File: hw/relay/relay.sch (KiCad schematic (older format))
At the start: 14 parts, among them J1 trigger input, J2 power input, J3 output terminal, K1 G5LE-1, Q1 PN2222A

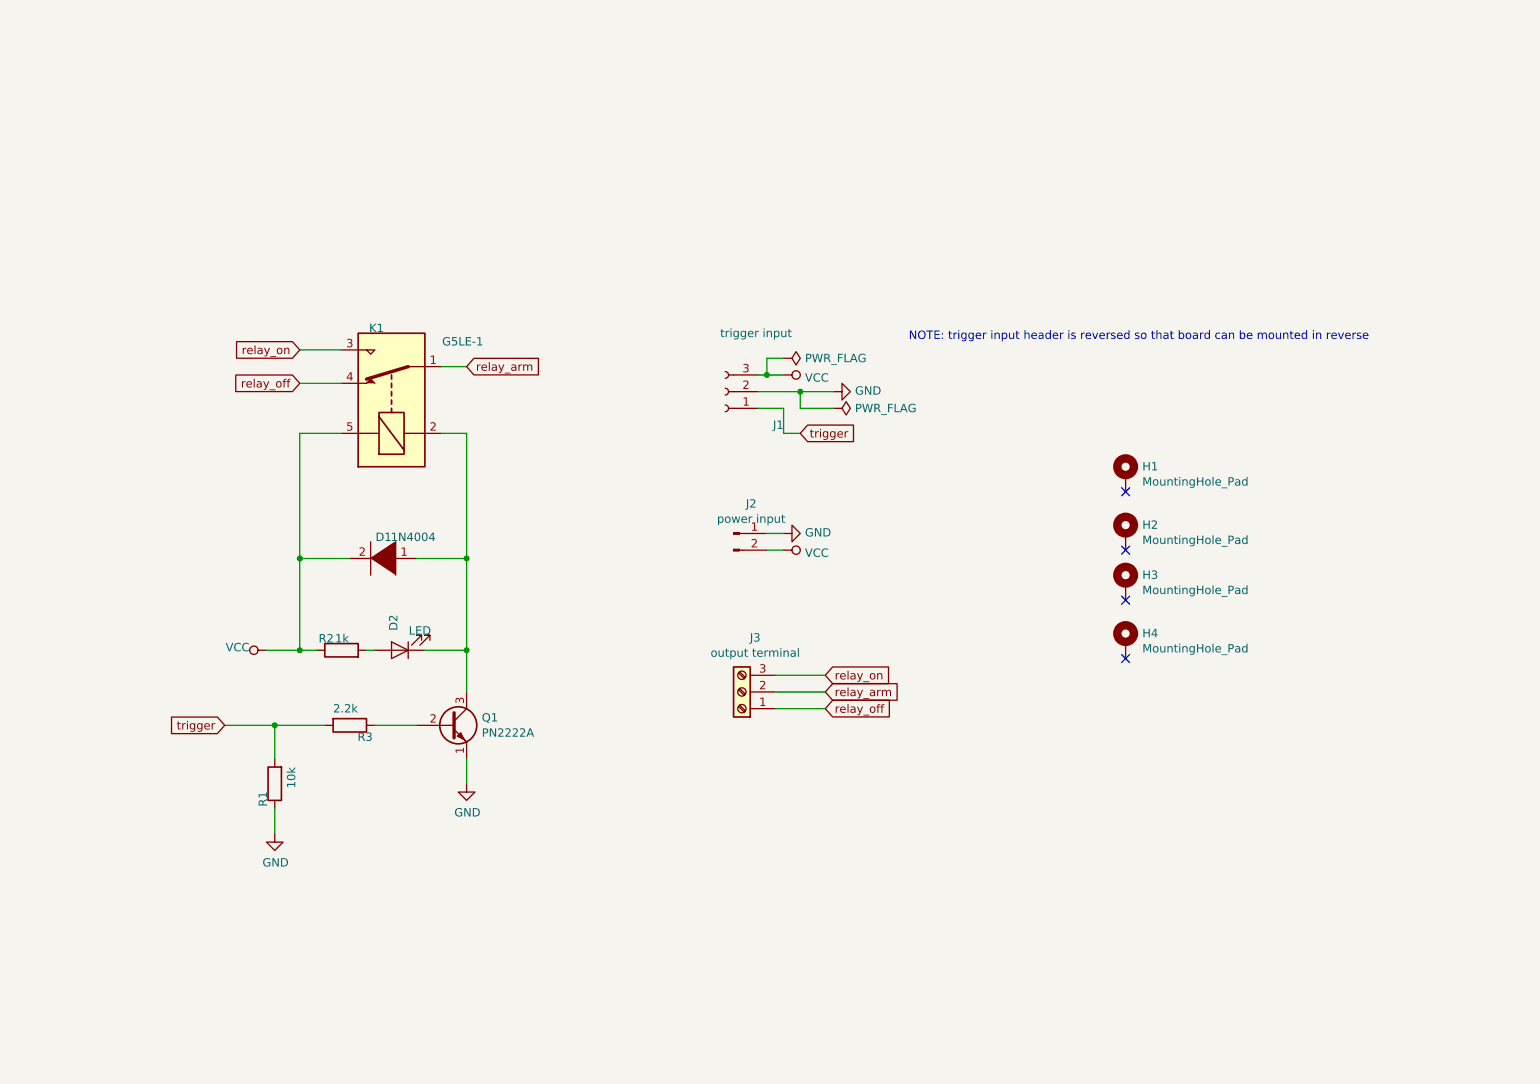
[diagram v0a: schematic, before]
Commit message: fix DELAY bus assigments
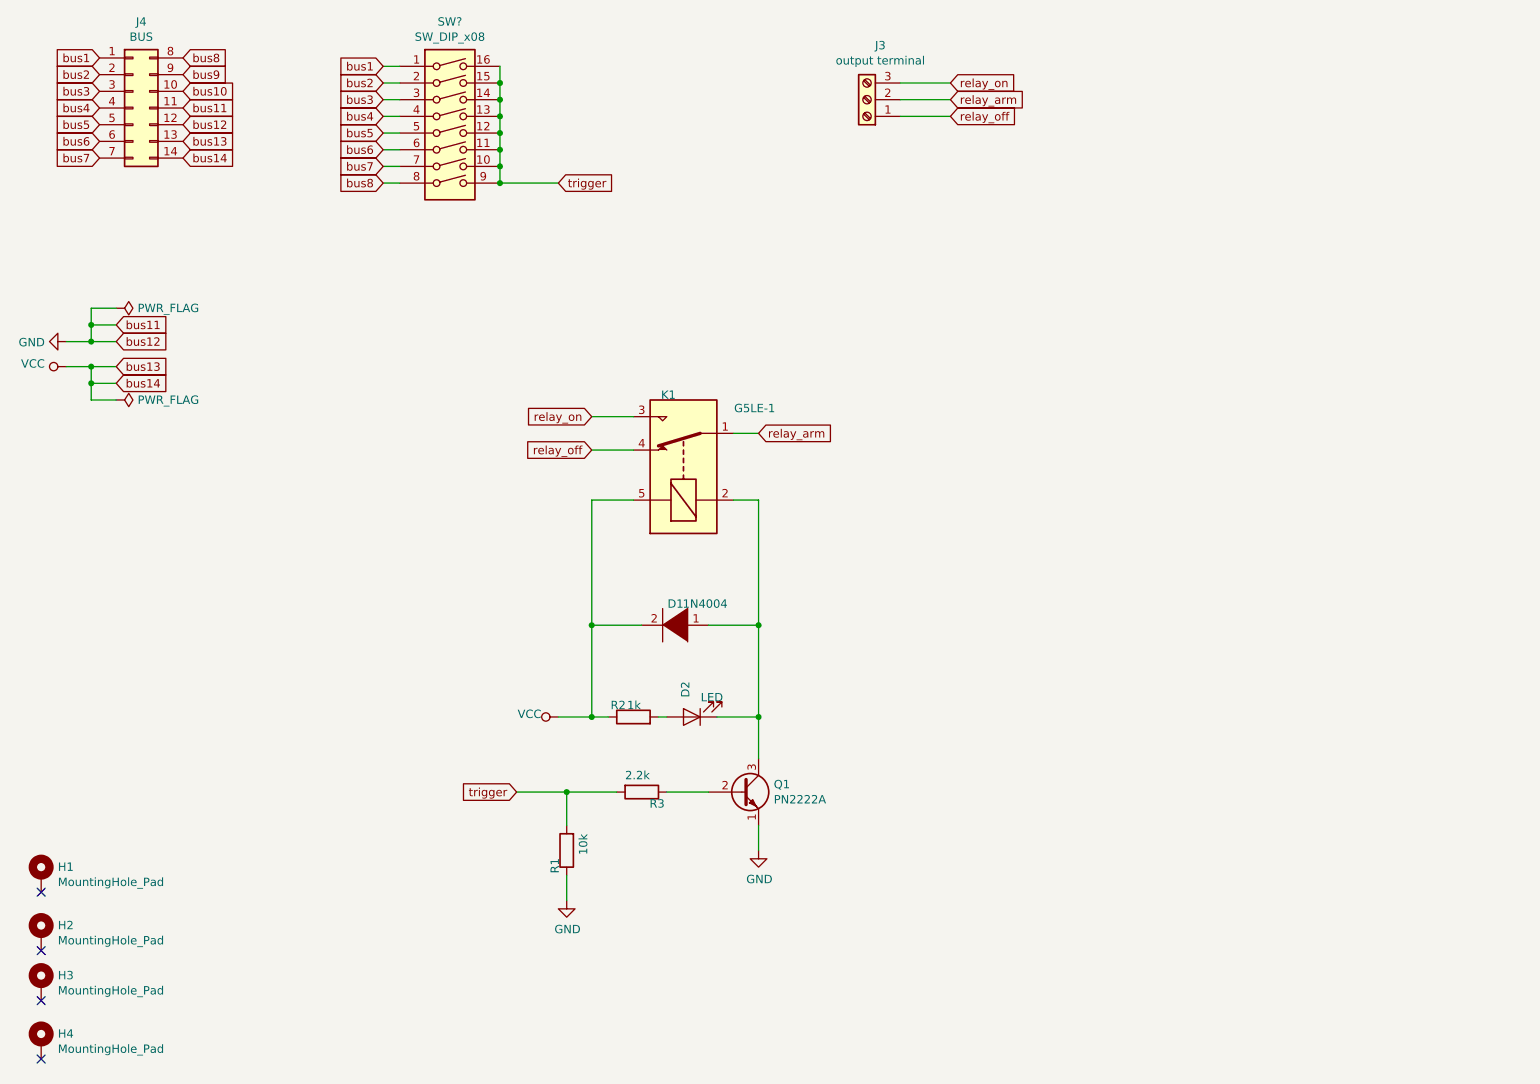
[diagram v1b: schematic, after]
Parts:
- removed J1: trigger input, Connector_PinHeader_2.54mm:PinHeader_1x03_P2.54mm_Vertical, symbol Connector:Conn_01x03_Female
- removed J2: power input, Connector_PinHeader_2.54mm:PinHeader_1x02_P2.54mm_Vertical, symbol Connector:Conn_01x02_Male
- added J4: BUS, symbol Connector_Generic:Conn_02x07_Top_Bottom
- added SW?: SW_DIP_x08, symbol Switch:SW_DIP_x08
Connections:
- net GND: now also J4.11 (Pin_11), J4.12 (Pin_12)
- net VCC: now also J4.13 (Pin_13), J4.14 (Pin_14)
- net trigger: now also SW?.10, SW?.11, SW?.12, SW?.13, SW?.14, SW?.15, SW?.16, SW?.9
- new net bus1: J4.1 (Pin_1), SW?.1
- new net bus10: J4.10 (Pin_10)
- new net bus2: J4.2 (Pin_2), SW?.2
- new net bus3: J4.3 (Pin_3), SW?.3
- new net bus4: J4.4 (Pin_4), SW?.4
- new net bus5: J4.5 (Pin_5), SW?.5
- new net bus6: J4.6 (Pin_6), SW?.6
- new net bus7: J4.7 (Pin_7), SW?.7
- new net bus8: J4.8 (Pin_8), SW?.8
- new net bus9: J4.9 (Pin_9)
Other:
- note removed: "NOTE: trigger input header is reversed so that board can be mounted in reverse"
- moved on the sheet: D1, D2, H1, H2, H3, H4, J3, K1, Q1, R1, R2, R3

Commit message: RELAY bus connection
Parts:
- added H5: MountingHole_Pad, MountingHole:MountingHole_3.5mm, symbol Mechanical:MountingHole_Pad
- J4: footprint (none) -> Connector_PinHeader_2.54mm:PinHeader_2x07_P2.54mm_Vertical
- SW1: renamed from SW?; footprint (none) -> Package_DIP:DIP-16_W7.62mm_SMDSocket_SmallPads
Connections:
- net bus1: no longer SW1.1
- net bus10: now also SW1.8
- net bus2: no longer SW1.2
- net bus3: now also SW1.1; no longer SW1.3
- net bus4: now also SW1.2; no longer SW1.4
- net bus5: now also SW1.3; no longer SW1.5
- net bus6: now also SW1.4; no longer SW1.6
- net bus7: now also SW1.5; no longer SW1.7
- net bus8: now also SW1.6; no longer SW1.8
- net bus9: now also SW1.7
- no-connect marks 4 -> 5
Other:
- moved on the sheet: SW1
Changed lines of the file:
@@
 F 0 "J4" H 1800 1917 50  0000 C CNN
 F 1 "BUS" H 1800 1826 50  0000 C CNN
-F 2 "" H 1750 1400 50  0001 C CNN
+F 2 "Connector_PinHeader_2.54mm:PinHeader_2x07_P2.54mm_Vertical" H 1750 1400 50  0001 C CNN
 F 3 "~" H 1750 1400 50  0001 C CNN
 	1    1750 1400
@@
 bus11
 $Comp
-L power:PWR_FLAG #FLG?
+L power:PWR_FLAG #FLG02
 U 1 1 5BFCA5F3
 P 1650 3150
-F 0 "#FLG?" H 1650 3225 50  0001 C CNN
+F 0 "#FLG02" H 1650 3225 50  0001 C CNN
 F 1 "PWR_FLAG" V 1650 3278 50  0000 L CNN
 F 2 "" H 1650 3150 50  0001 C CNN
@@
 $EndComp
 $Comp
-L power:PWR_FLAG #FLG?
+L power:PWR_FLAG #FLG01
 U 1 1 5BFCA61C
 P 1650 2600
-F 0 "#FLG?" H 1650 2675 50  0001 C CNN
+F 0 "#FLG01" H 1650 2675 50  0001 C CNN
 F 1 "PWR_FLAG" V 1650 2728 50  0000 L CNN
 F 2 "" H 1650 2600 50  0001 C CNN
@@
 $EndComp
 $Comp
-L power:VCC #PWR?
+L power:VCC #PWR05
 U 1 1 5BFCA645
 P 1350 2950
-F 0 "#PWR?" H 1350 2800 50  0001 C CNN
+F 0 "#PWR05" H 1350 2800 50  0001 C CNN
 F 1 "VCC" V 1367 3078 50  0000 L CNN
 F 2 "" H 1350 2950 50  0001 C CNN
@@
 $EndComp
 $Comp
-L power:GND #PWR?
+L power:GND #PWR04
 U 1 1 5BFCA70C
 P 1350 2800
-F 0 "#PWR?" H 1350 2550 50  0001 C CNN
+F 0 "#PWR04" H 1350 2550 50  0001 C CNN
 F 1 "GND" V 1355 2672 50  0000 R CNN
 F 2 "" H 1350 2800 50  0001 C CNN
@@
 	1500 3050 1500 3150
 $Comp
-L Switch:SW_DIP_x08 SW?
+L Switch:SW_DIP_x08 SW1
 U 1 1 5BFDB299
-P 3650 1550
-F 0 "SW?" H 3650 2217 50  0000 C CNN
-F 1 "SW_DIP_x08" H 3650 2126 50  0000 C CNN
-F 2 "" H 3650 1550 50  0001 C CNN
-F 3 "" H 3650 1550 50  0001 C CNN
-	1    3650 1550
+P 3900 1550
+F 0 "SW1" H 3900 2217 50  0000 C CNN
+F 1 "SW_DIP_x08" H 3900 2126 50  0000 C CNN
+F 2 "Package_DIP:DIP-16_W7.62mm_SMDSocket_SmallPads" H 3900 1550 50  0001 C CNN
+F 3 "" H 3900 1550 50  0001 C CNN
+	1    3900 1550
 	1    0    0    -1
 $EndComp
-Text GLabel 3250 1150 0    50   Input ~ 0
-bus1
-Text GLabel 3250 1250 0    50   Input ~ 0
-bus2
-Text GLabel 3250 1350 0    50   Input ~ 0
+Text GLabel 3500 1150 0    50   Input ~ 0
 bus3
-Text GLabel 3250 1450 0    50   Input ~ 0
+Text GLabel 3500 1250 0    50   Input ~ 0
 bus4
-Text GLabel 3250 1550 0    50   Input ~ 0
+Text GLabel 3500 1350 0    50   Input ~ 0
 bus5
-Text GLabel 3250 1650 0    50   Input ~ 0
+Text GLabel 3500 1450 0    50   Input ~ 0
 bus6
-Text GLabel 3250 1750 0    50   Input ~ 0
+Text GLabel 3500 1550 0    50   Input ~ 0
 bus7
 Wire Wire Line
-	3250 1150 3350 1150
+	3500 1150 3600 1150
 Wire Wire Line
-	3350 1250 3250 1250
+	3500 1250 3600 1250
 Wire Wire Line
-	3250 1350 3350 1350
+	3500 1350 3600 1350
 Wire Wire Line
-	3250 1450 3350 1450
+	3500 1450 3600 1450
 Wire Wire Line
-	3250 1550 3350 1550
+	3500 1550 3600 1550
 Wire Wire Line
-	3250 1650 3350 1650
-Wire Wire Line
-	3250 1750 3350 1750
-Text GLabel 3250 1850 0    50   Input ~ 0
+	3500 1650 3600 1650
+Text GLabel 3500 1650 0    50   Input ~ 0
 bus8
 Wire Wire Line
-	3250 1850 3350 1850
-Text GLabel 4300 1850 2    50   Input ~ 0
+	3500 1750 3600 1750
+Text GLabel 4550 1850 2    50   Input ~ 0
 trigger
 Wire Wire Line
-	3950 1150 3950 1250
-Connection ~ 3950 1250
+	4200 1150 4200 1250
+Connection ~ 4200 1250
 Wire Wire Line
-	3950 1250 3950 1350
-Connection ~ 3950 1350
+	4200 1250 4200 1350
+Connection ~ 4200 1350
 Wire Wire Line
-	3950 1350 3950 1450
-Connection ~ 3950 1450
+	4200 1350 4200 1450
+Connection ~ 4200 1450
 Wire Wire Line
-	3950 1450 3950 1550
-Connection ~ 3950 1550
+	4200 1450 4200 1550
+Connection ~ 4200 1550
 Wire Wire Line
-	3950 1550 3950 1650
-Connection ~ 3950 1650
+	4200 1550 4200 1650
+Connection ~ 4200 1650
 Wire Wire Line
-	3950 1650 3950 1750
-Connection ~ 3950 1750
+	4200 1650 4200 1750
+Connection ~ 4200 1750
 Wire Wire Line
-	3950 1750 3950 1850
+	4200 1750 4200 1850
 Wire Wire Line
-	3950 1850 4300 1850
-Connection ~ 3950 1850
+	4200 1850 4550 1850
+Connection ~ 4200 1850
+Text GLabel 3500 1750 0    50   Input ~ 0
+bus9
+Text GLabel 3500 1850 0    50   Input ~ 0
+bus10
+Wire Wire Line
+	3500 1850 3600 1850
+$Comp
+L Mechanical:MountingHole_Pad H5
+U 1 1 5C03D3D4
+P 2550 7050
+F 0 "H5" H 2650 7101 50  0000 L CNN
+F 1 "MountingHole_Pad" H 2650 7010 50  0000 L CNN
+F 2 "MountingHole:MountingHole_3.5mm" H 2550 7050 50  0001 C CNN
+F 3 "~" H 2550 7050 50  0001 C CNN
+	1    2550 7050
+	1    0    0    -1
+$EndComp
+NoConn ~ 2550 7150
 $EndSCHEMATC
